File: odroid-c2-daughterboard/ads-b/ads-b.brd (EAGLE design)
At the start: 64.8 x 56 mm, 46 parts, among them U1 SEN-09403, U3 BMP180

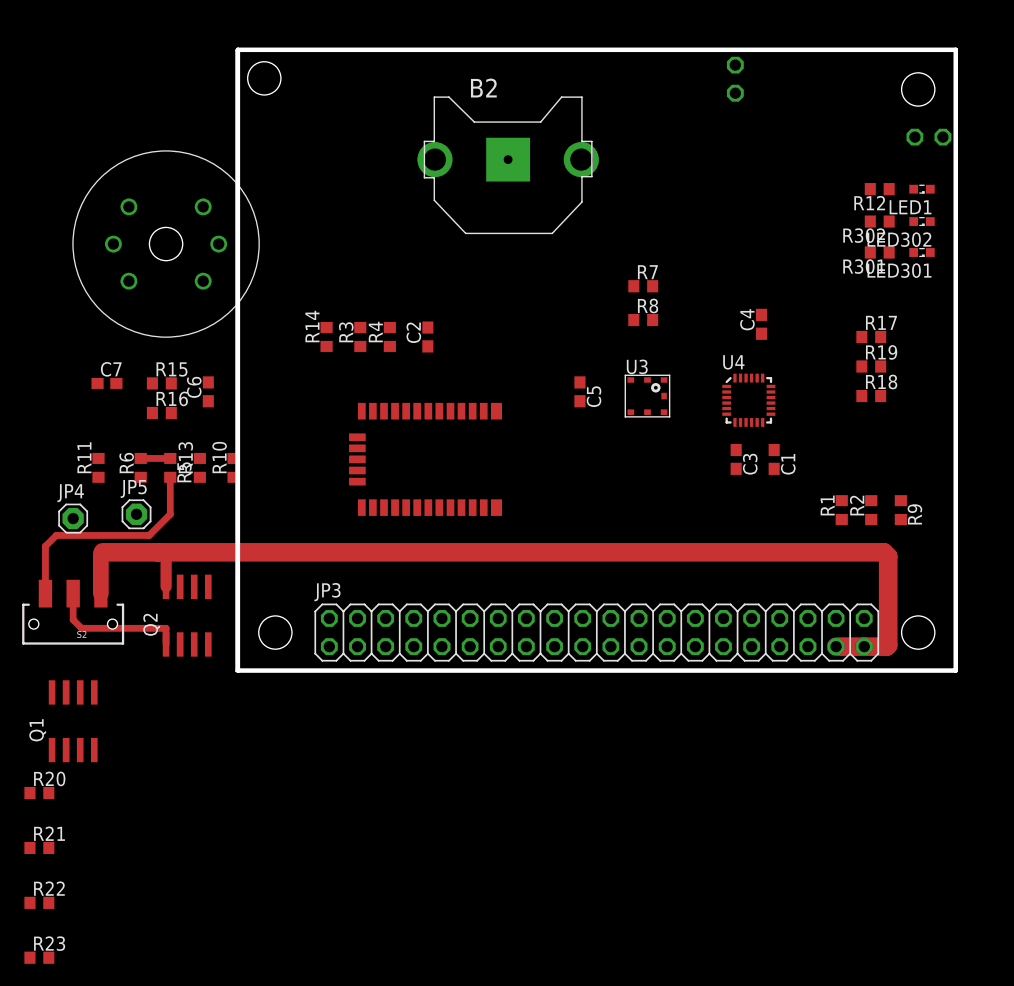
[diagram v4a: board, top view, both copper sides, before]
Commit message: ADS-B board sloppily laid out
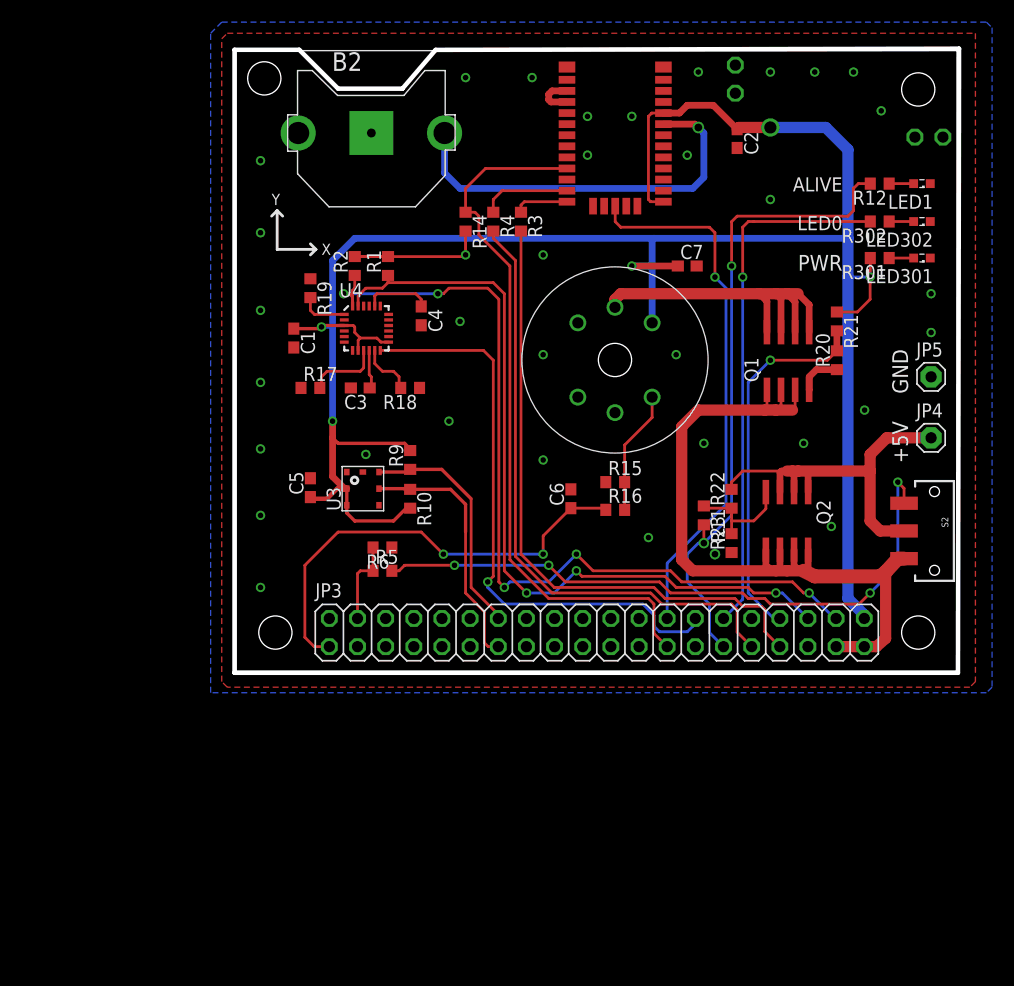
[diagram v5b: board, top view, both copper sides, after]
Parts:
- removed R13: 4.7k, rcl:R0603
- removed R7, R8: 10k, rcl:R0603
- moved R21 86.2 mm to (75.0, 31.5), turned to 270 degrees
- moved R20 81.9 mm to (75.0, 28.0), turned to 90 degrees
- moved S2 78.2 mm to (83.8, 12.6), turned to 270 degrees
- moved JP4 77.7 mm to (83.5, 21.0)
- moved R23 72.8 mm to (65.5, 11.5), turned to 90 degrees
- moved JP5 72.8 mm to (83.5, 26.5)
- moved R22 72.3 mm to (65.5, 15.5), turned to 90 degrees
- moved Q1 72.2 mm to (70.6, 27.9)
- moved Q2 54.8 mm to (70.5, 13.5), turned to 180 degrees
- moved R11 54.8 mm to (63.0, 14.0), turned to 270 degrees
- moved C7 53.4 mm to (61.5, 36.5)
- moved R2 51.5 mm to (31.5, 36.5)
- moved R19 51.1 mm to (27.5, 34.5), turned to 270 degrees
- moved R17 50.8 mm to (27.5, 25.5)
- moved R1 46.5 mm to (34.5, 36.5)
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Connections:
- net +3V3: no longer R7.2, R8.2
- net +5V: now also S2.3; no longer S2.1
- net GND: no longer JP3.P14, R13.1
- net HEATER_ENABLE: now also JP3.P7
- net I2CB_SCL: no longer R8.1
- net I2CB_SDA: no longer R7.1
- net KEEP_ALIVE: no longer R13.2
- net N$10: now also S2.1; no longer S2.3
- net N$2: now also B2.+2; no longer B2.+1
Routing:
- net +3V3: track 0.00 -> 212.0 mm, vias 0 -> 6
- net I2CA_SDA: track 0.00 -> 79.0 mm, vias 0 -> 5
- net I2CA_SCL: track 0.00 -> 71.5 mm, vias 0 -> 3
- net GPS_RESET: track 0.00 -> 64.5 mm
- net KEEP_ALIVE: track 0.00 -> 58.4 mm, vias 0 -> 2
- net GPS_RXD: track 0.00 -> 57.1 mm
- net GPS_TXD: track 0.00 -> 56.1 mm
- net IMU_INT: track 0.00 -> 53.0 mm, vias 0 -> 1
- net GPS_TIMEPULSE: track 0.00 -> 48.2 mm, vias 0 -> 1
- net USER_LED0: track 0.00 -> 47.7 mm, vias 0 -> 1
- net CO2_AD: track 0.00 -> 41.0 mm, vias 0 -> 2
- net N$10: track 19.8 -> 58.4 mm, vias 0 -> 4
- net N$2: track 0.00 -> 36.0 mm, vias 0 -> 1
- net HEATER_ENABLE: track 0.00 -> 33.8 mm, vias 0 -> 1
- net N$14: track 0.00 -> 32.5 mm
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- added copper zone on layer 1, net GND
- added copper zone on layer 16, net GND
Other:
- board size 64.8 x 56 mm -> 65.4 x 56.3 mm
- board text added: "+5V"
- board text added: "ALIVE"
- board text added: "GND"
- board text added: "LED0"
- board text added: "PWR"
- board text added: "X"
- board text added: "Y"
